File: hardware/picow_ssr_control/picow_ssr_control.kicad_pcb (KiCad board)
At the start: 2 copper layers, 65 x 90 mm, 44 parts, among them Q1 IRF4905PBF, Q2 DMG2301L, U1 RaspberryPi-PicoW

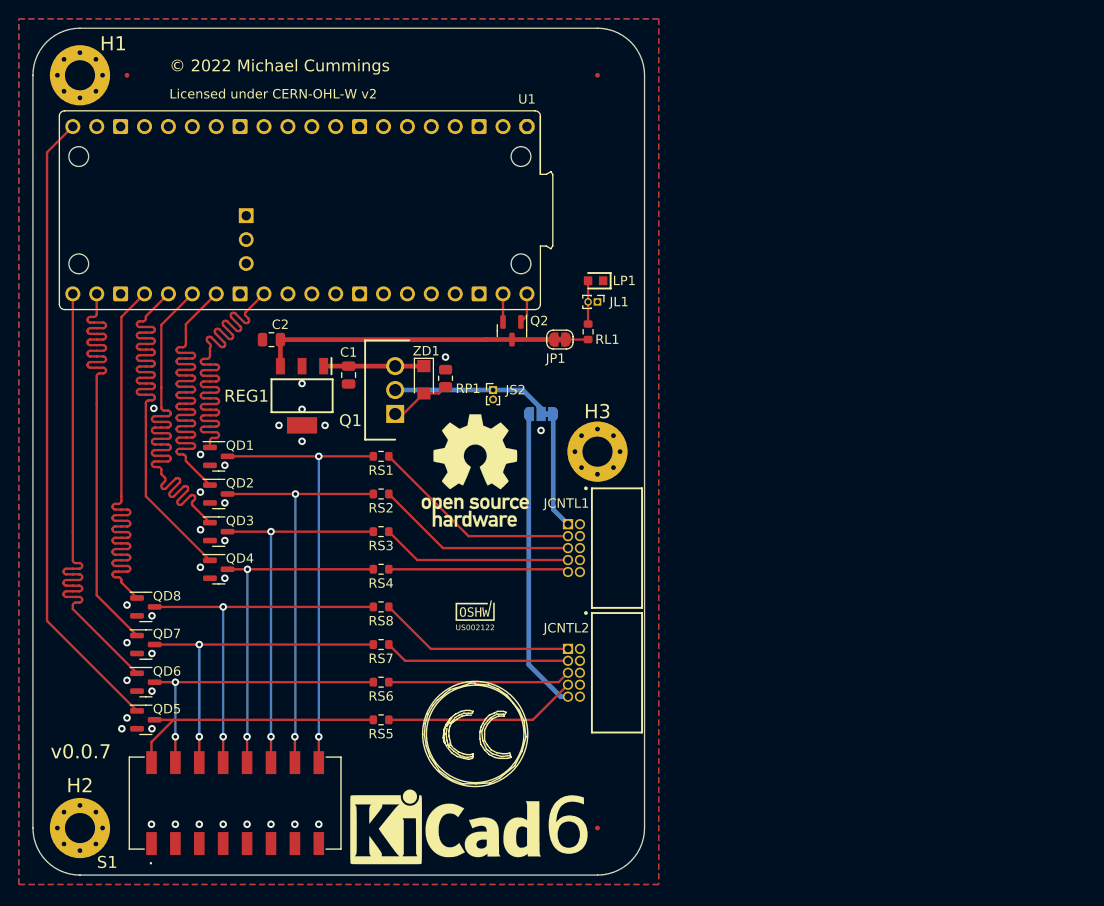
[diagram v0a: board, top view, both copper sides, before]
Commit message: Vertical Pico, Moved connectors, and draft production files
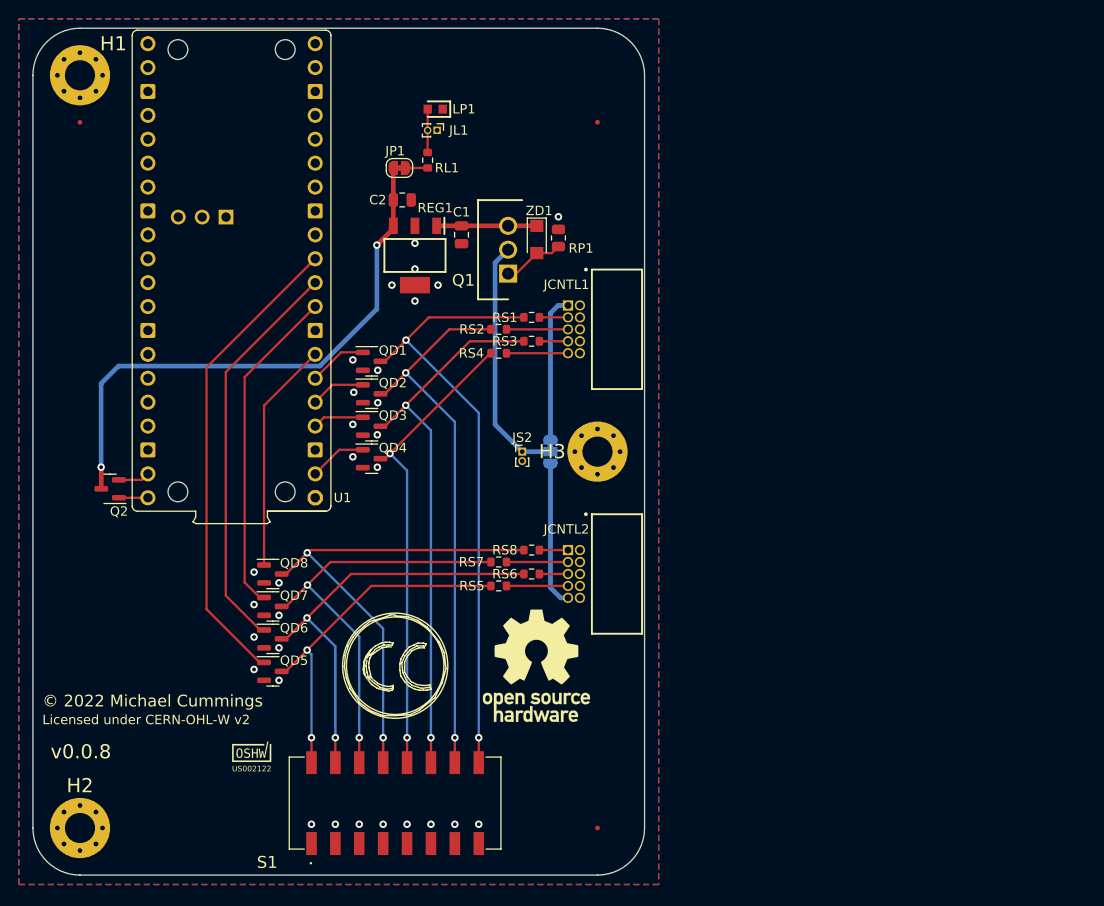
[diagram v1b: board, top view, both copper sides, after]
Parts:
- #LOGO2: moved to B.Cu
- moved Q2 45.9 mm to (24.7, 65.0), turned to 180 degrees
- moved U1 45.4 mm to (46.5, 65.9), turned to 180 degrees
- moved QRCode1 30.0 mm to (27.0, 78.8)
- moved OSHW_Mono_0.1_Scale 28.1 mm to (39.8, 92.9)
- moved RS4 26.1 mm to (66.0, 50.5)
- moved RS3 25.8 mm to (69.5, 49.3)
- moved RL1 25.0 mm to (58.5, 30.0)
- moved JL1 25.0 mm to (59.5, 26.9)
- moved JP1 25.0 mm to (55.5, 30.9)
- moved LP1 25.0 mm to (59.2, 24.6)
- moved JCNTL1 23.2 mm to (74.0, 48.0)
- moved RS1 21.8 mm to (69.5, 46.7)
- moved #LOGO1 21.7 mm to (70.0, 83.8)
- moved RS2 21.5 mm to (66.0, 48.0)
- moved C2 20.3 mm to (55.8, 34.2), turned to 0 degrees
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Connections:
- U1 pad 10: unconnected-(U1-Pad10) -> /b6
- U1 pad 11: unconnected-(U1-Pad11) -> /b5
- U1 pad 2: unconnected-(U1-Pad2) -> /b4
- U1 pad 20: /b5 -> unconnected-(U1-Pad20)
- U1 pad 21: /b6 -> unconnected-(U1-Pad21)
- U1 pad 22: /b7 -> unconnected-(U1-Pad22)
- U1 pad 24: /b8 -> unconnected-(U1-Pad24)
- U1 pad 25: /b4 -> unconnected-(U1-Pad25)
- U1 pad 26: /b3 -> unconnected-(U1-Pad26)
- U1 pad 27: /b2 -> unconnected-(U1-Pad27)
- U1 pad 29: /b1 -> unconnected-(U1-Pad29)
- U1 pad 4: unconnected-(U1-Pad4) -> /b3
- U1 pad 5: unconnected-(U1-Pad5) -> /b2
- U1 pad 6: unconnected-(U1-Pad6) -> /b1
- U1 pad 7: unconnected-(U1-Pad7) -> /b8
- U1 pad 9: unconnected-(U1-Pad9) -> /b7
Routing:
- net /b3: track 54.5 -> 5.45 mm
- net /b2: track 54.5 -> 5.82 mm
- net /b4: track 54.6 -> 6.12 mm
- net /b1: track 54.4 -> 6.20 mm
- net /b8: track 54.7 -> 24.6 mm
- net +5V: track 31.8 -> 59.3 mm, vias 0 -> 2
- net /b7: track 54.7 -> 34.7 mm
- net Net-(JCNTL1-Pad3): track 22.6 -> 3.04 mm
- net Net-(JCNTL2-Pad1): track 20.9 -> 3.04 mm
- net /a3: track 40.0 -> 57.6 mm
- net Net-(JCNTL1-Pad7): track 20.3 -> 3.04 mm
- net /b5: track 67.2 -> 50.0 mm
- net /a1: track 48.0 -> 64.8 mm
- net Net-(JCNTL2-Pad9): track 32.2 -> 15.5 mm
- net Net-(JCNTL2-Pad5): track 19.5 -> 3.04 mm
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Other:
- board text added: "v0.0.8"
- board text removed: "v0.0.7"

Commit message: Added pulldowns to driver FETs and realigned control connectors and other components
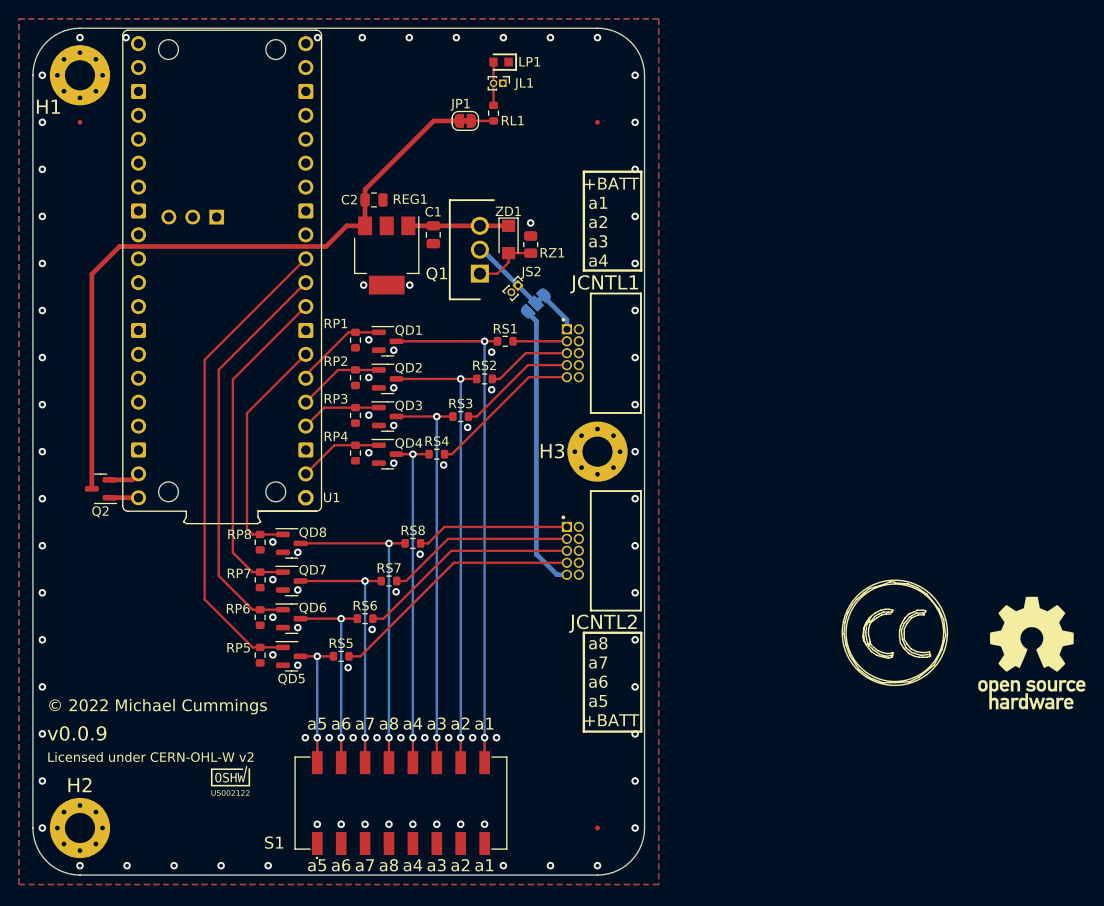
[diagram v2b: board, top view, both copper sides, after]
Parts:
- added RP2: 10k, Resistor_SMD:R_0603_1608Metric, F.Cu at (50.8, 53.1)
- added RP3: 10k, Resistor_SMD:R_0603_1608Metric, F.Cu at (50.8, 57.1)
- added RP4: 10k, Resistor_SMD:R_0603_1608Metric, F.Cu at (50.8, 61.1)
- added RP5: 10k, Resistor_SMD:R_0603_1608Metric, F.Cu at (40.6, 82.6)
- added RP6: 10k, Resistor_SMD:R_0603_1608Metric, F.Cu at (40.6, 78.6)
- added RP7: 10k, Resistor_SMD:R_0603_1608Metric, F.Cu at (40.6, 74.6)
- added RP8: 10k, Resistor_SMD:R_0603_1608Metric, F.Cu at (40.6, 70.6)
- added RZ1: 100k, Resistor_SMD:R_0805_2012Metric, F.Cu at (69.4, 39.0)
- OSHW_Mono_0.1_Scale: footprint Picow_control:OSHW_Mono_0.1_Scale -> dragon_mobile:OSHW_Mono_0.1_Scale
- Q2: footprint Picow_control:DMG2301L -> Package_TO_SOT_SMD:SOT-23
- REG1: footprint SamacSys_Parts:SOT230P700X180-4N -> Package_TO_SOT_SMD:SOT-223
- RP1: value 100k -> 10k; footprint Resistor_SMD:R_0805_2012Metric -> Resistor_SMD:R_0603_1608Metric
- S1: footprint Picow_control:1938MS -> dragon_mobile:1938MS
- U1: footprint Pico:Raspberry_Pi_Pico_THT -> dragon_mobile:Raspberry_Pi_Pico_THT
- ZD1: footprint Picow_control:BZD27C10P-M3-08 -> dragon_mobile:BZD27C10P-M3-08
- moved #LOGO2 53.2 mm to (108.1, 80.2)
- moved #LOGO1 52.7 mm to (122.7, 82.4)
- moved RP1 24.1 mm to (50.8, 49.1), turned to -90 degrees
- moved RS5 18.3 mm to (49.3, 82.8)
- moved RS6 18.3 mm to (51.8, 78.8)
- moved JS2 17.7 mm to (68.1, 43.3), turned to -45 degrees
- moved JS1 15.8 mm to (70.0, 45.2), turned to -135 degrees
- moved RS8 12.6 mm to (56.9, 70.8)
- moved RS4 12.6 mm to (59.4, 61.3)
- moved RS7 11.8 mm to (54.3, 74.8)
- moved RS3 11.0 mm to (62.0, 57.3)
- moved JL1 8.60 mm to (66.5, 21.9)
- moved JP1 8.60 mm to (62.5, 25.9)
- moved LP1 8.60 mm to (66.2, 19.6)
- moved RL1 8.60 mm to (65.5, 25.0)
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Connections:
- RP1 pad 1: Net-(Q1-Pad1) -> /b1
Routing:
- net /a6: track 44.8 -> 21.3 mm
- net /a5: track 37.7 -> 14.8 mm
- net Net-(JCNTL2-Pad7): track 6.54 -> 27.3 mm
- net Net-(JCNTL2-Pad5): track 3.04 -> 23.6 mm
- net +BATT: track 26.2 -> 8.32 mm
- net /a8: track 52.0 -> 34.4 mm
- net /a7: track 44.9 -> 27.9 mm
- net /a3: track 57.6 -> 42.8 mm
- net Net-(JCNTL2-Pad9): track 15.5 -> 30.3 mm
- net Net-(JCNTL2-Pad3): track 6.54 -> 19.9 mm
- net Net-(JCNTL2-Pad1): track 3.04 -> 16.3 mm
- net /a4: track 49.5 -> 36.3 mm
- net +5V: track 59.3 -> 70.9 mm, vias 2 -> 0
- net Net-(JCNTL1-Pad1): track 15.6 -> 4.66 mm
- net Net-(JCNTL1-Pad9): track 6.54 -> 16.4 mm
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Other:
- board text added: "+BATT a1 a2 a3 a4"
- board text added: "JCNTL1"
- board text added: "JCNTL2"
- board text added: "a1"
- board text added: "a2"
- board text added: "a3"
- board text added: "a4"
- board text added: "a5"
- board text added: "a6"
- board text added: "a7"
- board text added: "a8"
- board text added: "a8 a7 a6 a5 +BATT"
- board text added: "v0.0.9"
- board text removed: "v0.0.8"

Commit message: Changed schematic to hierarchical style with mutliple sheets
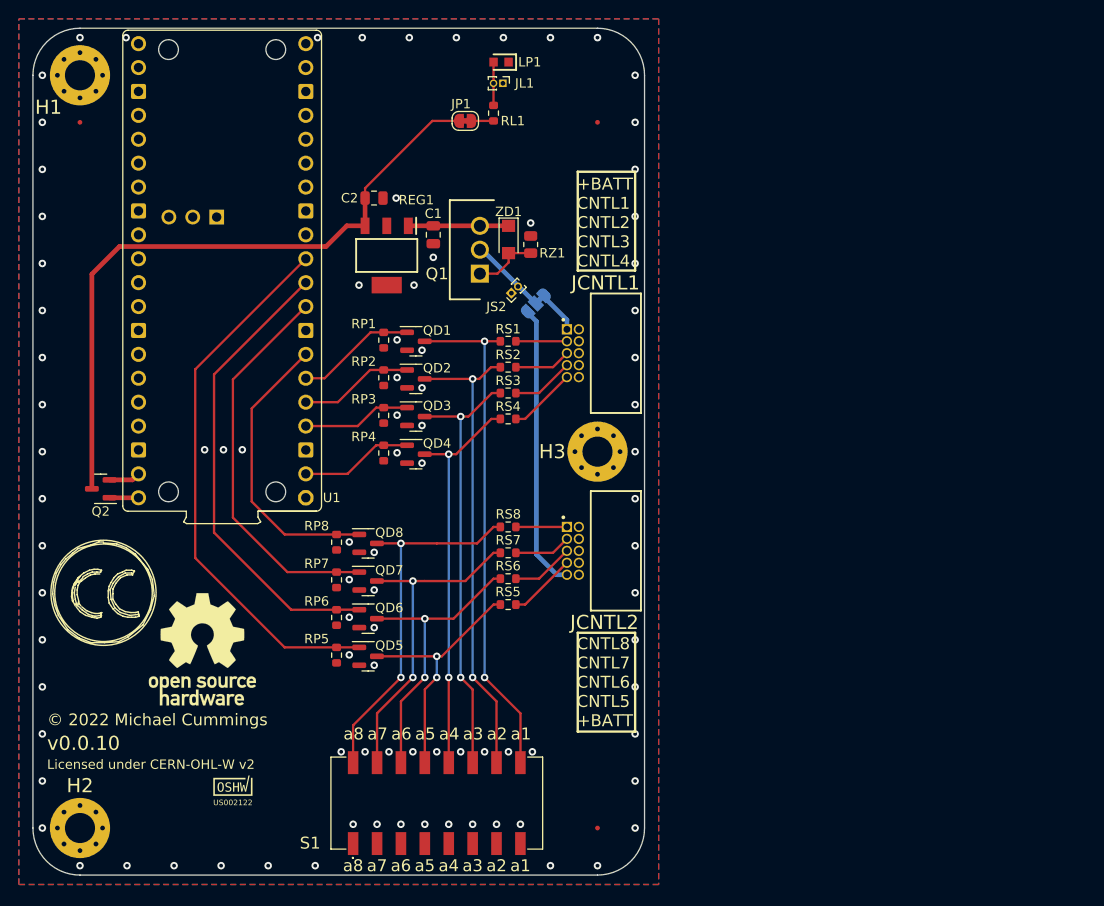
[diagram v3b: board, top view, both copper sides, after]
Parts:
- REG1: footprint Package_TO_SOT_SMD:SOT-223 -> SamacSys_Parts:SOT230P700X180-4N
- moved #LOGO1 88.2 mm to (34.5, 82.0)
- moved #LOGO2 84.2 mm to (24.0, 76.0)
- moved RS5 18.6 mm to (67.0, 77.2)
- moved RS6 15.8 mm to (67.0, 74.5)
- moved RS7 13.0 mm to (67.0, 71.8)
- moved RS8 10.3 mm to (67.0, 69.0)
- moved RS4 8.46 mm to (67.0, 57.5)
- moved RP5 8.12 mm to (48.8, 82.6)
- moved RP6 8.12 mm to (48.8, 78.6)
- moved RP7 8.12 mm to (48.8, 74.6)
- moved RP8 8.12 mm to (48.8, 70.6)
- moved QD5 8.12 mm to (52.1, 82.8)
- moved QD6 8.12 mm to (52.1, 78.8)
- moved QD7 8.12 mm to (52.1, 74.8)
- moved QD8 8.12 mm to (52.1, 70.8)
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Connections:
- net /a1 renamed /Control Out/BANK_A.CNTL1
- net /a2 renamed /Control Out/BANK_A.CNTL2
- net /a3 renamed /Control Out/BANK_A.CNTL3
- net /a4 renamed /Control Out/BANK_A.CNTL4
- net /b1 renamed /Pico W Control/IO1
- net /b2 renamed /Pico W Control/IO2
- net /b3 renamed /Pico W Control/IO3
- net /b4 renamed /Pico W Control/IO4
- net /b5 renamed /Pico W Control/IO5
- net /b6 renamed /Pico W Control/IO6
- net /b7 renamed /Pico W Control/IO7
- net /b8 renamed /Pico W Control/IO8
- net Net-(JCNTL1-Pad1) renamed /Control Out/PwrIn1
- net Net-(JCNTL1-Pad3) renamed /Control Out/a1o
- net Net-(JCNTL1-Pad5) renamed /Control Out/a2o
- net Net-(JCNTL1-Pad7) renamed /Control Out/a3o
- net Net-(JCNTL1-Pad9) renamed /Control Out/a4o
- net Net-(JCNTL2-Pad1) renamed /Control Out/a8o
- net Net-(JCNTL2-Pad3) renamed /Control Out/a7o
- net Net-(JCNTL2-Pad5) renamed /Control Out/a6o
- net Net-(JCNTL2-Pad7) renamed /Control Out/a5o
- net Net-(JCNTL2-Pad9) renamed /Control Out/PwrIn2
- net Net-(Q2-Pad1) renamed /Pico W Control/VBUS
- net Net-(Q2-Pad2) renamed /Pico W Control/VSYS
- JS2 pad 1: +BATT -> GNDPWR
- JS2 pad 2: GNDPWR -> +BATT
- QD5 pad 3: /a5 -> /Control Out/BANK_B.CNTL5
- QD6 pad 3: /a6 -> /Control Out/BANK_B.CNTL6
- QD7 pad 3: /a7 -> /Control Out/BANK_B.CNTL7
- QD8 pad 3: /a8 -> /Control Out/BANK_B.CNTL8
- RS5 pad 1: /a5 -> /Control Out/BANK_B.CNTL5
- RS6 pad 1: /a6 -> /Control Out/BANK_B.CNTL6
- RS7 pad 1: /a7 -> /Control Out/BANK_B.CNTL7
- RS8 pad 1: /a8 -> /Control Out/BANK_B.CNTL8
- S1 pad 13: /a8 -> /Control Out/BANK_B.CNTL5
- S1 pad 14: /a7 -> /Control Out/BANK_B.CNTL6
- S1 pad 15: /a6 -> /Control Out/BANK_B.CNTL7
- S1 pad 16: /a5 -> /Control Out/BANK_B.CNTL8
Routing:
- net /Control Out/BANK_B.CNTL8: track 0.00 -> 39.2 mm, vias 0 -> 2
- net /Control Out/BANK_B.CNTL7: track 0.00 -> 35.2 mm, vias 0 -> 2
- net /a8: track 34.4 -> 0.00 mm, vias 2 -> 0
- net /Control Out/BANK_B.CNTL6: track 0.00 -> 31.2 mm, vias 0 -> 2
- net /a7: track 27.9 -> 0.00 mm, vias 2 -> 0
- net /Control Out/BANK_B.CNTL5: track 0.00 -> 27.2 mm, vias 0 -> 2
- net /a6: track 21.3 -> 0.00 mm, vias 2 -> 0
- net /Control Out/a5o: track 27.3 -> 7.26 mm
- net /Control Out/a6o: track 23.6 -> 6.65 mm
- net /a5: track 14.8 -> 0.00 mm, vias 2 -> 0
- net /Control Out/a7o: track 19.9 -> 6.04 mm
- net /Control Out/a8o: track 16.3 -> 5.42 mm
- net /Control Out/a4o: track 16.4 -> 7.26 mm
- net /Pico W Control/IO5: track 51.1 -> 58.0 mm
- net /Pico W Control/IO6: track 43.3 -> 49.4 mm
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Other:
- board text added: "+BATT CNTL1 CNTL2 CNTL3 CNTL4"
- board text added: "CNTL8 CNTL7 CNTL6 CNTL5 +BATT"
- board text added: "v0.0.10"
- board text removed: "+BATT a1 a2 a3 a4"
- board text removed: "a8 a7 a6 a5 +BATT"
- board text removed: "v0.0.9"

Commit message: Updated schemas
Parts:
- added C3: 100n, Capacitor_SMD:C_0805_2012Metric, F.Cu at (24.8, 62.4)
- Q2: value DMG2301L -> DMG2305UX-7
- REG1: footprint SamacSys_Parts:SOT230P700X180-4N -> Package_TO_SOT_SMD:SOT-223
- RZ1: footprint Resistor_SMD:R_0805_2012Metric -> Resistor_SMD:R_0603_1608Metric
- moved #LOGO2 66.7 mm to (63.5, 29.6)
- moved Q2 2.63 mm to (21.1, 64.3)
- moved QD5 1.75 mm to (52.1, 81.0)
- moved QD6 1.75 mm to (52.1, 77.0)
- moved QD7 1.75 mm to (52.1, 73.0)
- moved QD8 1.75 mm to (52.1, 69.0)
- moved RP5 1.75 mm to (48.8, 80.9)
- moved RP6 1.75 mm to (48.8, 76.9)
- moved RP7 1.75 mm to (48.8, 72.9)
- moved RP8 1.75 mm to (48.8, 68.9)
- moved RZ1 0.09 mm to (69.4, 39.1)
- turned RS4 to 0 degrees
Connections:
- net +VDC renamed /Power Management/VDC
- RS4 pad 1: /Control Out/a4o -> /Control Out/BANK_A.CNTL4
- RS4 pad 2: /Control Out/BANK_A.CNTL4 -> /Control Out/a4o
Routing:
- net /Pico W Control/IO5: track 58.0 -> 55.0 mm
- net /Pico W Control/VBUS: track 3.08 -> 5.90 mm
- net /Pico W Control/VSYS: track 3.35 -> 5.63 mm
- net /Pico W Control/IO6: track 49.4 -> 47.6 mm
- net /Pico W Control/IO7: track 41.5 -> 40.1 mm
- net /Control Out/BANK_B.CNTL8: track 39.2 -> 40.3 mm
- net /Control Out/BANK_B.CNTL7: track 35.2 -> 36.3 mm
- net /Control Out/BANK_B.CNTL6: track 31.2 -> 32.3 mm
- net /Control Out/BANK_B.CNTL5: track 27.2 -> 28.2 mm
- net /Pico W Control/IO8: track 30.9 -> 30.2 mm
- net GNDPWR: vias 92 -> 93
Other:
- board text added: "A1"
- board text added: "A2"
- board text added: "A3"
- board text added: "A4"
- board text added: "B5"
- board text added: "B6"
- board text added: "B7"
- board text added: "B8"
- board text removed: "JCNTL1"
- board text removed: "JCNTL2"
- board text removed: "a1"
- board text removed: "a2"
- board text removed: "a3"
- board text removed: "a4"
- board text removed: "a5"
- board text removed: "a6"
- board text removed: "a7"
- board text removed: "a8"

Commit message: Power supply changes plus misc.
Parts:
- removed the #LOGO2 at (63.5, 29.6)
- removed REG1: LM7805, Package_TO_SOT_SMD:SOT-223
- removed RZ1: 100k, Resistor_SMD:R_0603_1608Metric
- added C10: 4u7, Capacitor_SMD:C_0805_2012Metric, F.Cu at (57.5, 32.1)
- added C11: 100n, Capacitor_SMD:C_0603_1608Metric, F.Cu at (24.8, 62.6)
- added C4: 1u, Capacitor_SMD:C_0603_1608Metric, F.Cu at (64.2, 25.9)
- added C5: 100n, Capacitor_SMD:C_0603_1608Metric, F.Cu at (59.0, 26.9)
- added C6: 4u7, Capacitor_SMD:C_0805_2012Metric, F.Cu at (57.5, 42.5)
- added C7: 4u7, Capacitor_SMD:C_0805_2012Metric, F.Cu at (57.5, 39.8)
- added C8: 4u7, Capacitor_SMD:C_0805_2012Metric, F.Cu at (57.5, 37.2)
- added C9: 4u7, Capacitor_SMD:C_0805_2012Metric, F.Cu at (57.5, 34.7)
- added L1: 2u2, Inductor_SMD:L_1008_2520Metric, F.Cu at (56.5, 29.0)
- added R1: 100k, Resistor_SMD:R_0603_1608Metric, F.Cu at (73.1, 32.2)
- added R2: 100k, Resistor_SMD:R_0603_1608Metric, F.Cu at (63.5, 23.5)
- added R3: 100k, Resistor_SMD:R_0603_1608Metric, F.Cu at (66.5, 29.0)
- added R4: 24k9, Resistor_SMD:R_0603_1608Metric, F.Cu at (68.2, 29.0)
- added REF_KiCAD: KiCad-Logo2_5mm_SilkScreen, Symbol:KiCad-Logo2_5mm_SilkScreen, B.Cu at (59.4, 97.0)
- added U2: LMR33610BDDAR, Package_SO:Texas_HSOP-8-1EP_3.9x4.9mm_P1.27mm_ThermalVias, F.Cu at (62.8, 30.9)
- C1: value 330n -> 4u7
- C2: value 100n -> 4u7
- C3: value 100n -> 220n; footprint Capacitor_SMD:C_0805_2012Metric -> Capacitor_SMD:C_0603_1608Metric
- JL1, JS2: footprint Connector_PinHeader_1.00mm:PinHeader_1x02_P1.00mm_Vertical -> dragon_mobile:PinHeader_1x02_P1.00mm_Vertical
- Q1: value IRF4905PBF -> SQ3419EV-T1_GE3; footprint dragon_mobile:TO254P469X1042X1967-3P -> dragon_mobile:SOT95P284X110-6N
- RL1, RS1, RS2, RS3, RS4, RS5, RS6, RS7, RS8: value 270 -> 270R
- ZD1: value +10v Zener Diode -> 10V; footprint dragon_mobile:BZD27C10P-M3-08 -> Diode_SMD:D_0805_2012Metric
- moved C3 45.6 mm to (62.2, 36.4), turned to -90 degrees
- moved C2 11.7 mm to (64.2, 36.5), turned to -90 degrees
- moved JP1 9.41 mm to (71.8, 26.3)
- moved Q1 9.04 mm to (71.2, 36.5), turned to 180 degrees
- moved C1 7.97 mm to (66.9, 36.5)
- moved ZD1 6.46 mm to (70.6, 33.1), turned to 0 degrees
- moved RL1 6.29 mm to (71.7, 24.1), turned to 180 degrees
- moved JL1 5.40 mm to (71.8, 22.0)
- moved LP1 5.40 mm to (71.7, 19.6)
- moved JS2 3.87 mm to (71.0, 42.8), turned to 90 degrees
- moved FID1 2.50 mm to (21.5, 28.5)
- moved FID2 2.50 mm to (76.5, 28.5)
- moved Q2 2.05 mm to (21.9, 62.4), turned to 90 degrees
- moved JS1 2.02 mm to (72.0, 45.5), turned to 180 degrees
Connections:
- C2 pad 1: +5V -> /Power Management/VDC
- C3 pad 1: /Pico W Control/VSYS -> /Power Management/VDC
- Q1 pad 1: Net-(Q1-Pad1) -> +BATT
- Q1 pad 3: /Power Management/VDC -> Net-(Q1-Pad3)
- U1 pad 30: unconnected-(U1-Pad30) -> /Pico W Control/PG
- ZD1 pad 2: Net-(Q1-Pad1) -> Net-(Q1-Pad3)
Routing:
- net /Pico W Control/PG: track 0.00 -> 60.7 mm, vias 0 -> 2
- net +5V: track 71.4 -> 93.5 mm, vias 0 -> 2
- net Net-(Q1-Pad1): track 6.89 -> 0.00 mm
- net /Power Management/BOOT: track 0.00 -> 4.77 mm
- net Net-(Q1-Pad3): track 0.00 -> 4.32 mm
- net /Power Management/VCC: track 0.00 -> 3.82 mm
- net /Power Management/FB: track 0.00 -> 3.46 mm
- net /Power Management/VDC: track 10.6 -> 13.6 mm
- net /Pico W Control/VBUS: track 5.90 -> 8.38 mm
- net /Control Out/PwrIn1: track 4.37 -> 2.50 mm
- net +BATT: track 8.08 -> 7.23 mm, vias 0 -> 6
- net /Pico W Control/VSYS: track 5.63 -> 4.82 mm
- net GNDPWR: vias 93 -> 183
- added copper zone on B.Cu, net +BATT
- added copper zone on F.Cu, net +BATT
- added copper zone on F.Cu, net /Power Management/SW
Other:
- board text added: "v0.0.11"
- board text added: "© 2023 Michael Cummings"
- board text removed: "6"
- board text removed: "v0.0.10"
- board text removed: "© 2022 Michael Cummings"
